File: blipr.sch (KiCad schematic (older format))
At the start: 1 part

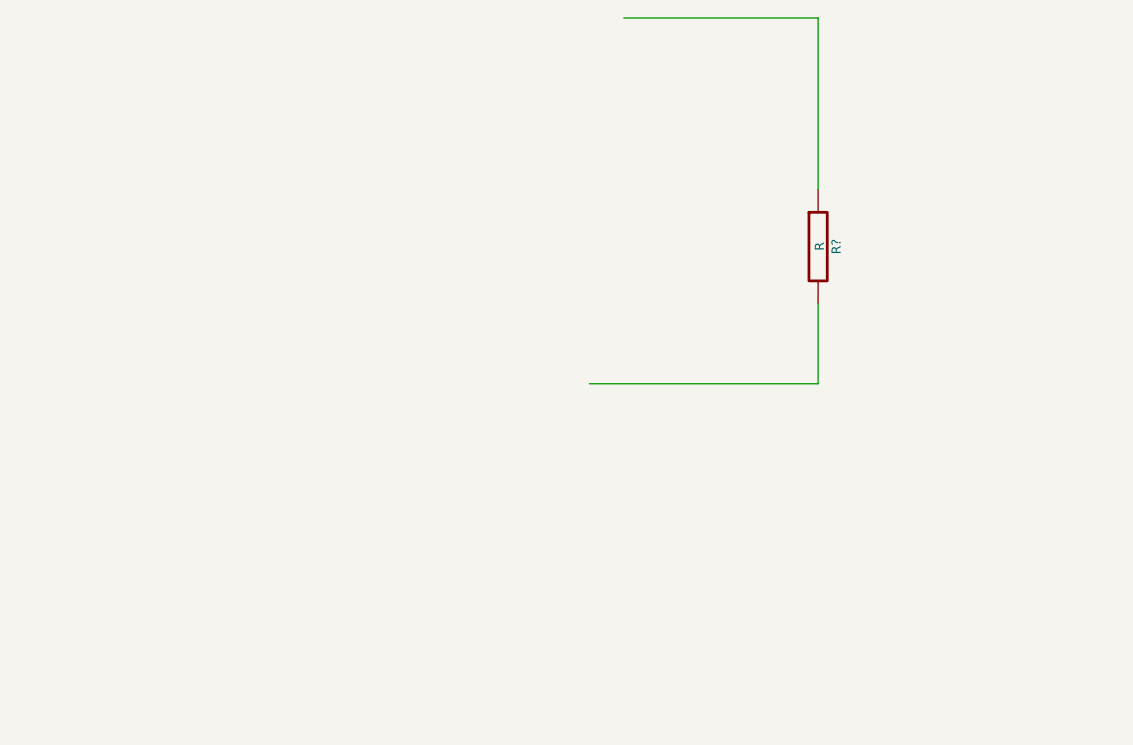
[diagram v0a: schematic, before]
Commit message: Added AY-3-8910 symbol
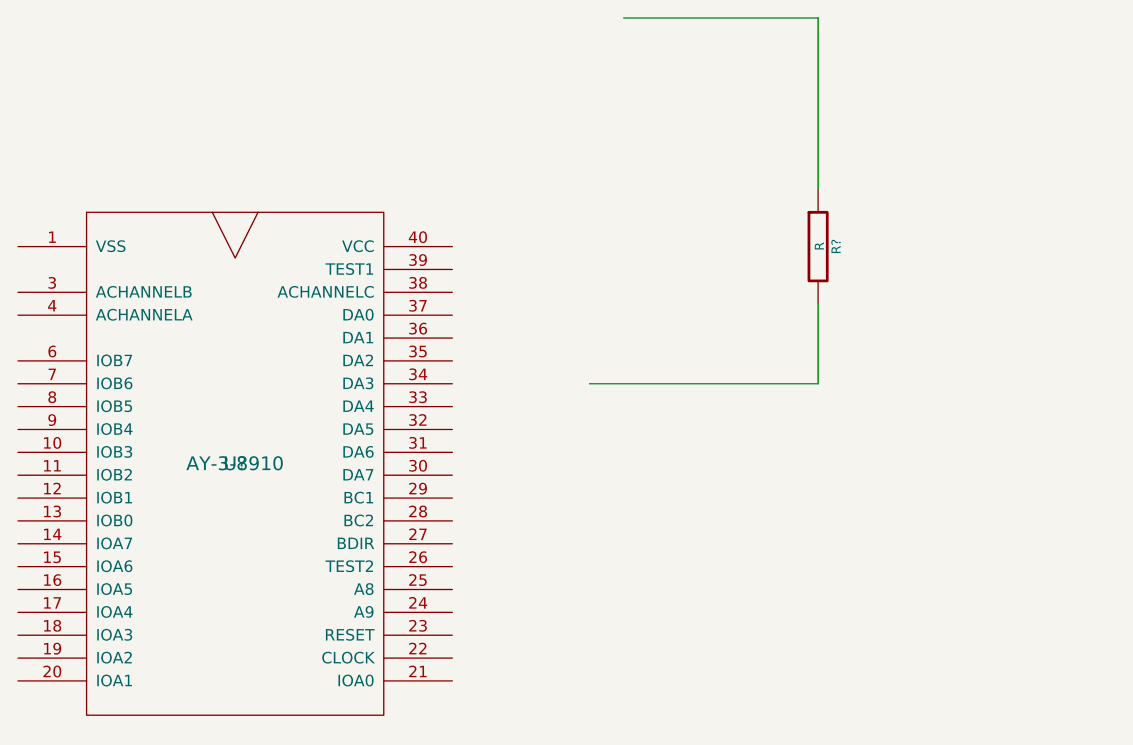
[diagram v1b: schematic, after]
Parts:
- added U?: AY-3-8910, ~, symbol AY-3-8910
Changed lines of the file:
@@
-EESchema Schematic File Version 2  date 02/03/2014 18:41:16
+EESchema Schematic File Version 2  date 02/03/2014 18:52:32
 LIBS:power
 LIBS:device
@@
 LIBS:contrib
 LIBS:valves
+LIBS:blipr-lib
+LIBS:blipr-cache
 EELAYER 27 0
 EELAYER END
@@
 Wire Wire Line
 	7000 3550 6000 3550
+$Comp
+L AY-3-8910 U?
+U 1 1 53136FF6
+P 4450 3900
+F 0 "U?" H 4450 3900 60  0000 C CNN
+F 1 "AY-3-8910" H 4450 3900 60  0000 C CNN
+F 2 "~" H 4450 3900 60  0000 C CNN
+F 3 "~" H 4450 3900 60  0000 C CNN
+	1    4450 3900
+	1    0    0    -1
+$EndComp
 $EndSCHEMATC

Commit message: Hej
hej
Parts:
- removed R?: R, ~, symbol R
- gave numbers to parts that had none: 1
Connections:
- wire segments 4 -> 12
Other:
- moved on the sheet: U1
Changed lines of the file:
@@
-EESchema Schematic File Version 2  date 02/03/2014 18:52:32
+EESchema Schematic File Version 2  date 02/03/2014 19:15:03
 LIBS:power
 LIBS:device
@@
 $EndDescr
 $Comp
-L R R?
-U 1 1 53136D33
-P 7000 2950
-F 0 "R?" V 7080 2950 40  0000 C CNN
-F 1 "R" V 7007 2951 40  0000 C CNN
-F 2 "~" V 6930 2950 30  0000 C CNN
-F 3 "~" H 7000 2950 30  0000 C CNN
-	1    7000 2950
+L AY-3-8910 U1
+U 1 1 53136FF6
+P 6500 3850
+F 0 "U1" H 6500 3850 60  0000 C CNN
+F 1 "AY-3-8910" H 6500 3850 60  0000 C CNN
+F 2 "~" H 6500 3850 60  0000 C CNN
+F 3 "~" H 6500 3850 60  0000 C CNN
+	1    6500 3850
 	1    0    0    -1
 $EndComp
 Wire Wire Line
-	7000 2700 7000 1950
+	5550 2900 4900 2900
 Wire Wire Line
-	7000 1950 6150 1950
+	7450 2900 8150 2900
+Entry Wire Line
+	7450 3500 7550 3600
+Wire Bus Line
+	7550 4000 8300 4000
+Entry Wire Line
+	7450 3400 7550 3500
+Entry Wire Line
+	7450 3300 7550 3400
+Entry Wire Line
+	7450 3200 7550 3300
+Entry Wire Line
+	7450 3600 7550 3700
+Entry Wire Line
+	7450 3700 7550 3800
+Entry Wire Line
+	7450 3800 7550 3900
+Entry Wire Line
+	7450 3900 7550 4000
+Wire Bus Line
+	7550 4000 7550 3300
+Entry Wire Line
+	5450 3400 5550 3500
+Entry Wire Line
+	5450 3800 5550 3900
+Entry Wire Line
+	5450 3900 5550 4000
+Entry Wire Line
+	5450 4000 5550 4100
+Entry Wire Line
+	5450 4200 5550 4300
+Entry Wire Line
+	5450 4300 5550 4400
+Entry Wire Line
+	5450 4500 5550 4600
+Entry Wire Line
+	5450 4600 5550 4700
+Entry Wire Line
+	5450 4700 5550 4800
+Wire Bus Line
+	5450 4100 5450 4800
+Wire Bus Line
+	5450 4100 5000 4100
+Wire Bus Line
+	5450 4000 5450 3300
+Wire Bus Line
+	5450 3300 4900 3300
+Entry Wire Line
+	5450 3300 5550 3400
+Entry Wire Line
+	5450 3500 5550 3600
+Entry Wire Line
+	5450 3600 5550 3700
+Entry Wire Line
+	5450 3700 5550 3800
+Entry Wire Line
+	5450 4100 5550 4200
+Entry Wire Line
+	5450 4400 5550 4500
 Wire Wire Line
-	7000 3200 7000 3550
+	7450 4600 8250 4600
 Wire Wire Line
-	7000 3550 6000 3550
-$Comp
-L AY-3-8910 U?
-U 1 1 53136FF6
-P 4450 3900
-F 0 "U?" H 4450 3900 60  0000 C CNN
-F 1 "AY-3-8910" H 4450 3900 60  0000 C CNN
-F 2 "~" H 4450 3900 60  0000 C CNN
-F 3 "~" H 4450 3900 60  0000 C CNN
-	1    4450 3900
-	1    0    0    -1
-$EndComp
+	7450 4700 8250 4700
+Wire Wire Line
+	7450 4800 7500 4800
+Wire Wire Line
+	7500 4800 7500 5050
+Wire Wire Line
+	7500 5050 5550 5050
+Wire Wire Line
+	5550 5050 5550 4900
+Entry Wire Line
+	5450 4800 5550 4900
+Wire Wire Line
+	5550 3100 4900 3100
+Wire Wire Line
+	5550 3200 4900 3200
+Wire Wire Line
+	7450 3000 8150 3000
+Wire Wire Line
+	7450 3100 8150 3100
 $EndSCHEMATC
